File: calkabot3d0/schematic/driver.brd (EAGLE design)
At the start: 60.9 x 42.9 mm, 56 parts

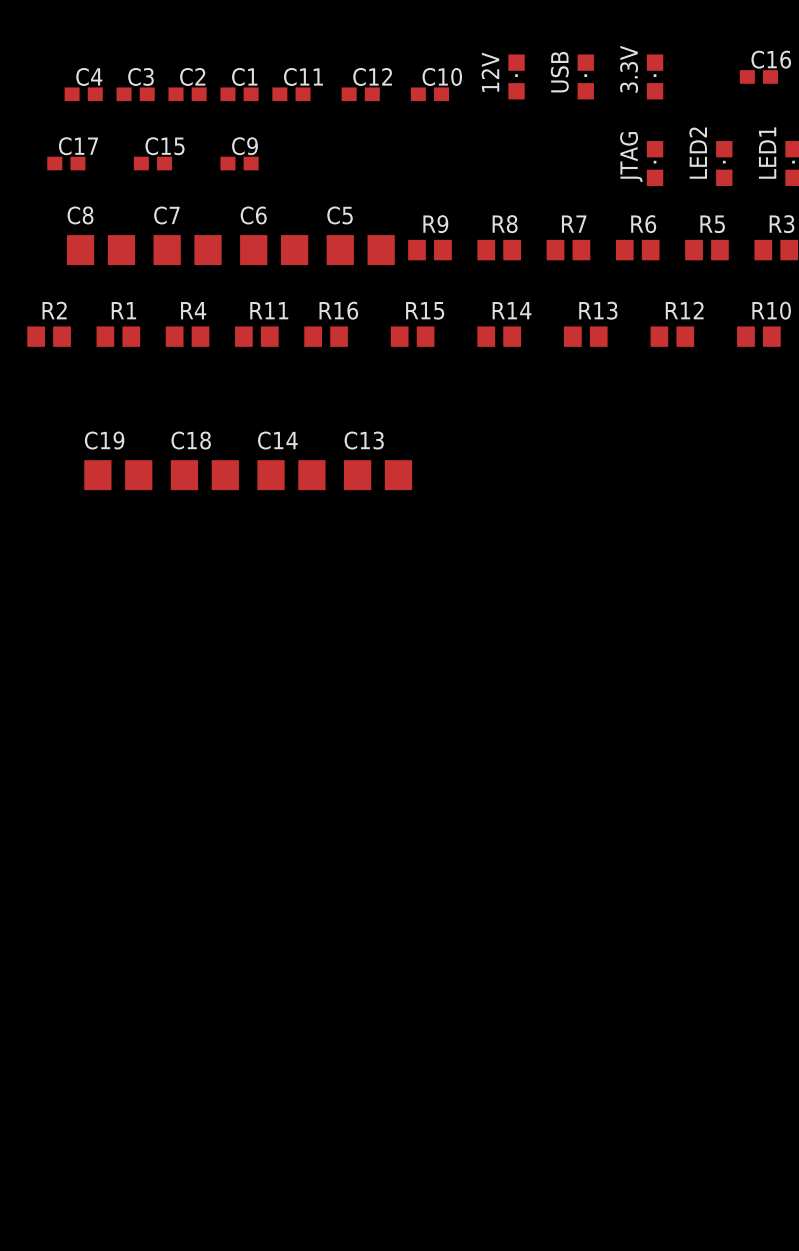
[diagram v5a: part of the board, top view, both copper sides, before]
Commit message: added battery voltage checker and led
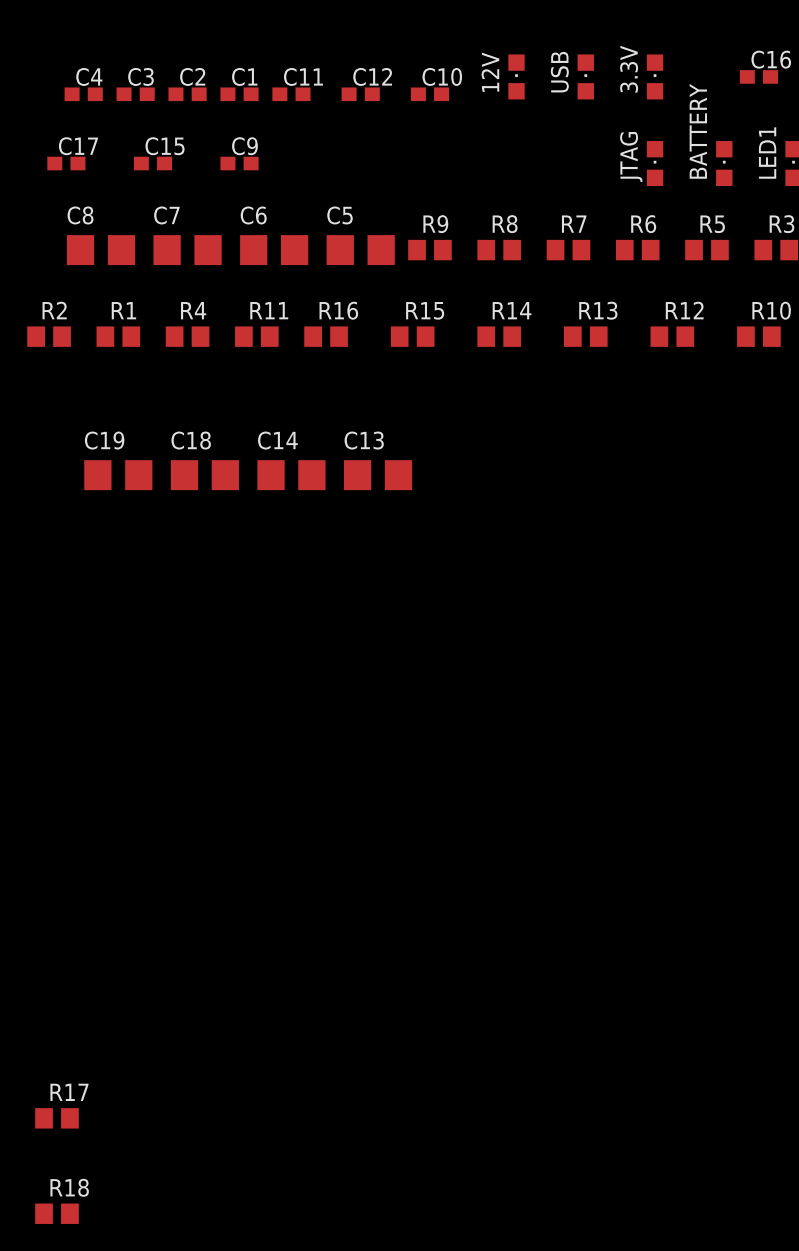
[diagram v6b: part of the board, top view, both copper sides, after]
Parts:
- added R17: 10k, rcl:R0805
- added R18: 30k, rcl:R0805
- renumbered LED2 to BATTERY
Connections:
- removed net S5: STM32.13
- new net BAT: R17.1, R18.2, STM32.13
- net GND: now also R18.1
- net STAB: now also R17.2
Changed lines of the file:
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@@
 <attribute name="VALUE" x="-11.43" y="64.77" size="1.27" layer="27" rot="R90"/>
 </element>
-<element name="LED2" library="led" library_urn="urn:adsk.eagle:library:259" package="CHIPLED_0805" package3d_urn="urn:adsk.eagle:package:15821/2" override_package3d_urn="urn:adsk.eagle:package:17628446/2" override_package_urn="urn:adsk.eagle:footprint:15685/1" value="" x="-19.05" y="66.04" smashed="yes">
+<element name="BATTERY" library="led" library_urn="urn:adsk.eagle:library:259" package="CHIPLED_0805" package3d_urn="urn:adsk.eagle:package:15821/2" override_package3d_urn="urn:adsk.eagle:package:17628446/2" override_package_urn="urn:adsk.eagle:footprint:15685/1" value="" x="-19.05" y="66.04" smashed="yes">
 <attribute name="NAME" x="-20.32" y="64.77" size="1.27" layer="25" rot="R90"/>
 <attribute name="POPULARITY" value="52" x="0" y="0" size="1.778" layer="27" display="off"/>
@@
 <attribute name="SPICEPREFIX" value="D" x="0" y="0" size="1.778" layer="27" display="off"/>
 <attribute name="VALUE" x="-26.67" y="71.12" size="1.27" layer="27" rot="R90"/>
+</element>
+<element name="R17" library="rcl" library_urn="urn:adsk.eagle:library:334" package="R0805" package3d_urn="urn:adsk.eagle:package:23553/2" value="10k" x="-68" y="-4" smashed="yes">
+<attribute name="NAME" x="-68.635" y="-2.73" size="1.27" layer="25"/>
+<attribute name="POPULARITY" value="86" x="-68" y="-4" size="1.778" layer="27" display="off"/>
+<attribute name="SPICEPREFIX" value="R" x="-68" y="-4" size="1.778" layer="27" display="off"/>
+<attribute name="VALUE" x="-68.635" y="-6.54" size="1.27" layer="27"/>
+</element>
+<element name="R18" library="rcl" library_urn="urn:adsk.eagle:library:334" package="R0805" package3d_urn="urn:adsk.eagle:package:23553/2" value="30k" x="-68" y="-11" smashed="yes">
+<attribute name="NAME" x="-68.635" y="-9.73" size="1.27" layer="25"/>
+<attribute name="POPULARITY" value="86" x="-68" y="-11" size="1.778" layer="27" display="off"/>
+<attribute name="SPICEPREFIX" value="R" x="-68" y="-11" size="1.778" layer="27" display="off"/>
+<attribute name="VALUE" x="-68.635" y="-13.54" size="1.27" layer="27"/>
 </element>
 </elements>
@@
 <contactref element="J2" pad="-"/>
 <contactref element="LED1" pad="C"/>
-<contactref element="LED2" pad="C"/>
+<contactref element="BATTERY" pad="C"/>
 <contactref element="JTAG" pad="C"/>
 <contactref element="USB" pad="C"/>
@@
 <wire x1="49.9826" y1="21.0174" x2="53" y2="18" width="1" layer="16"/>
 <wire x1="53" y1="18" x2="57" y2="18" width="1" layer="16"/>
+<contactref element="R18" pad="1"/>
 <wire x1="55.6166" y1="32.4485" x2="47.26" y2="35.29" width="0" layer="19" extent="1-1"/>
 <wire x1="30.48" y1="39.37" x2="47.26" y2="35.29" width="0" layer="19" extent="1-1"/>
@@
 <wire x1="-49.3" y1="43.18" x2="-55.65" y2="43.18" width="0" layer="19" extent="1-1"/>
 <wire x1="-42.95" y1="43.18" x2="-49.3" y2="43.18" width="0" layer="19" extent="1-1"/>
+<wire x1="-68.95" y1="-11" x2="-62" y2="43.18" width="0" layer="19" extent="1-1"/>
 </signal>
 <signal name="N$1">
@@
 <wire x1="57.51" y1="11.94" x2="58.94" y2="11.94" width="1" layer="16"/>
 <wire x1="58.94" y1="11.94" x2="59.424" y2="12.424" width="1" layer="16"/>
-<wire x1="-45.95" y1="43.18" x2="32.02" y2="35.29" width="0" layer="19" extent="1-1"/>
-<wire x1="-58.65" y1="43.18" x2="-45.95" y2="43.18" width="0" layer="19" extent="1-1"/>
+<contactref element="R17" pad="2"/>
+<wire x1="-58.65" y1="43.18" x2="-67.05" y2="-4" width="0" layer="19" extent="1-1"/>
 <wire x1="-57.47" y1="53.34" x2="-58.65" y2="43.18" width="0" layer="19" extent="1-1"/>
+<wire x1="-45.95" y1="43.18" x2="-58.65" y2="43.18" width="0" layer="19" extent="1-1"/>
+<wire x1="32.02" y1="35.29" x2="-45.95" y2="43.18" width="0" layer="19" extent="1-1"/>
 </signal>
 <signal name="LED1">
@@
 <contactref element="STM32" pad="14"/>
 </signal>
-<signal name="S5">
+<signal name="BAT">
 <contactref element="STM32" pad="13"/>
+<contactref element="R17" pad="1"/>
+<contactref element="R18" pad="2"/>
+<wire x1="-68.95" y1="-4" x2="-67.05" y2="-11" width="0" layer="19" extent="1-1"/>
+<wire x1="2.493478125" y1="50.767434375" x2="-68.95" y2="-4" width="0" layer="19" extent="1-16"/>
 </signal>
 <signal name="SWDA">
@@
 </signal>
 <signal name="N$8">
-<contactref element="LED2" pad="A"/>
+<contactref element="BATTERY" pad="A"/>
 <contactref element="R13" pad="1"/>
 <wire x1="-30.16" y1="53.34" x2="-19.05" y2="64.99" width="0" layer="19" extent="1-1"/>

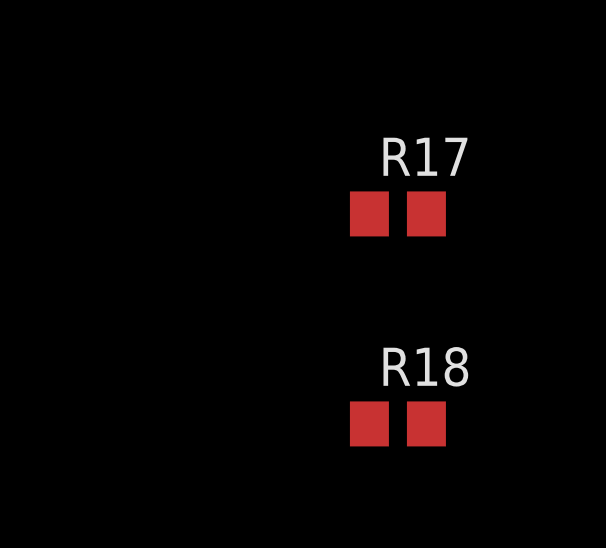
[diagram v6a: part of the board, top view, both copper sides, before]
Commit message: added switch to disconnect voltage from sensors
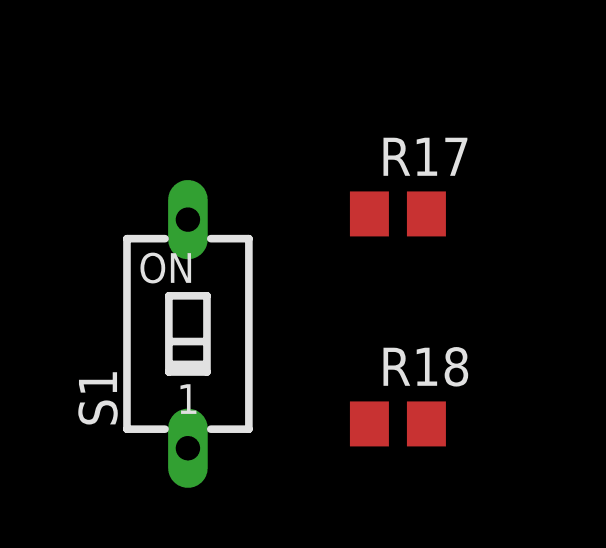
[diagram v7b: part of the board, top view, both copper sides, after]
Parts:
- added S1: (no value), switch-dil:SD4-01
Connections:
- new net VCC_S: I2C.4, S1.1
- net VCC: now also S1.2; no longer I2C.4
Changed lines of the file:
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@@
 <attribute name="VALUE" x="-68.635" y="-13.54" size="1.27" layer="27"/>
+</element>
+<element name="S1" library="switch-dil" library_urn="urn:adsk.eagle:library:375" package="SD4-01" package3d_urn="urn:adsk.eagle:package:27236/1" value="" x="-75" y="-8" smashed="yes">
+<attribute name="MF" value="" x="-75" y="-8" size="1.778" layer="27" display="off"/>
+<attribute name="MPN" value="" x="-75" y="-8" size="1.778" layer="27" display="off"/>
+<attribute name="NAME" x="-77.3622" y="-11.1242" size="1.27" layer="25" ratio="10" rot="R90"/>
+<attribute name="OC_FARNELL" value="unknown" x="-75" y="-8" size="1.778" layer="27" display="off"/>
+<attribute name="OC_NEWARK" value="unknown" x="-75" y="-8" size="1.778" layer="27" display="off"/>
+<attribute name="VALUE" x="-71.3678" y="-11.1496" size="1.27" layer="27" ratio="10" rot="R90"/>
 </element>
 </elements>
@@
 <contactref element="LM1" pad="4"/>
 <contactref element="C19" pad="+"/>
-<contactref element="I2C" pad="4"/>
 <contactref element="R16" pad="2"/>
 <contactref element="R15" pad="2"/>
 <wire x1="57.51" y1="14.24" x2="51.71" y2="14.24" width="1" layer="16"/>
+<contactref element="S1" pad="2"/>
 <wire x1="39.64" y1="22.59" x2="44.72" y2="35.29" width="0" layer="19" extent="1-1"/>
 <wire x1="51.71" y1="14.24" x2="39.64" y2="22.59" width="0" layer="19" extent="16-16"/>
-<wire x1="27.94" y1="39.37" x2="44.72" y2="35.29" width="0" layer="19" extent="1-1"/>
-<wire x1="-40.96" y1="53.34" x2="27.94" y2="39.37" width="0" layer="19" extent="1-1"/>
+<wire x1="-40.96" y1="53.34" x2="39.64" y2="22.59" width="0" layer="19" extent="1-1"/>
 <wire x1="-47.31" y1="53.34" x2="-40.96" y2="53.34" width="0" layer="19" extent="1-1"/>
 <wire x1="-65" y1="43.18" x2="-47.31" y2="53.34" width="0" layer="19" extent="1-1"/>
+<wire x1="-75" y1="-4.19" x2="-65" y2="43.18" width="0" layer="19" extent="1-1"/>
 </signal>
 <signal name="N$42">
@@
 <wire x1="-36.51" y1="59.69" x2="-29.21" y2="71.34" width="0" layer="19" extent="1-1"/>
 </signal>
+<signal name="VCC_S">
+<contactref element="S1" pad="1"/>
+<contactref element="I2C" pad="4"/>
+<wire x1="27.94" y1="39.37" x2="-75" y2="-11.81" width="0" layer="19" extent="1-1"/>
+</signal>
 </signals>

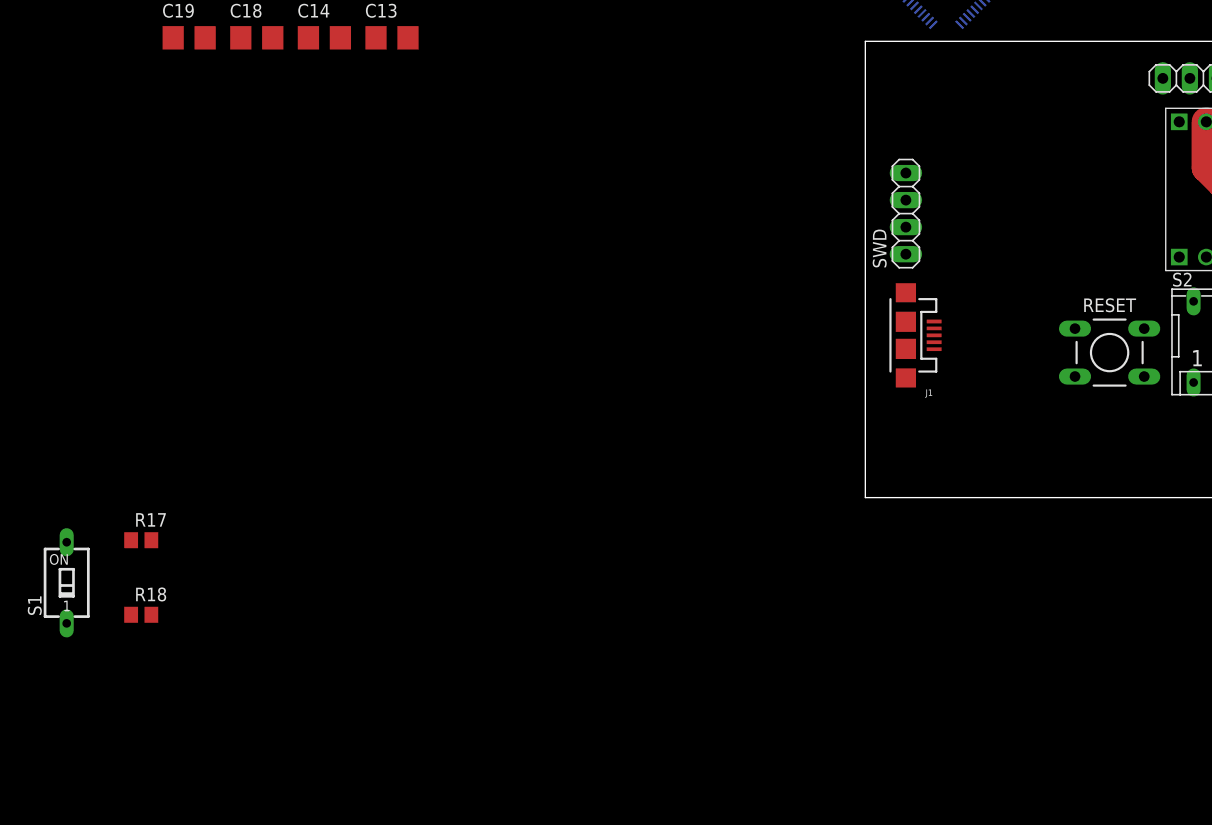
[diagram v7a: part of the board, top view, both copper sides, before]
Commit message: comments on schematic, added led for I2C supply
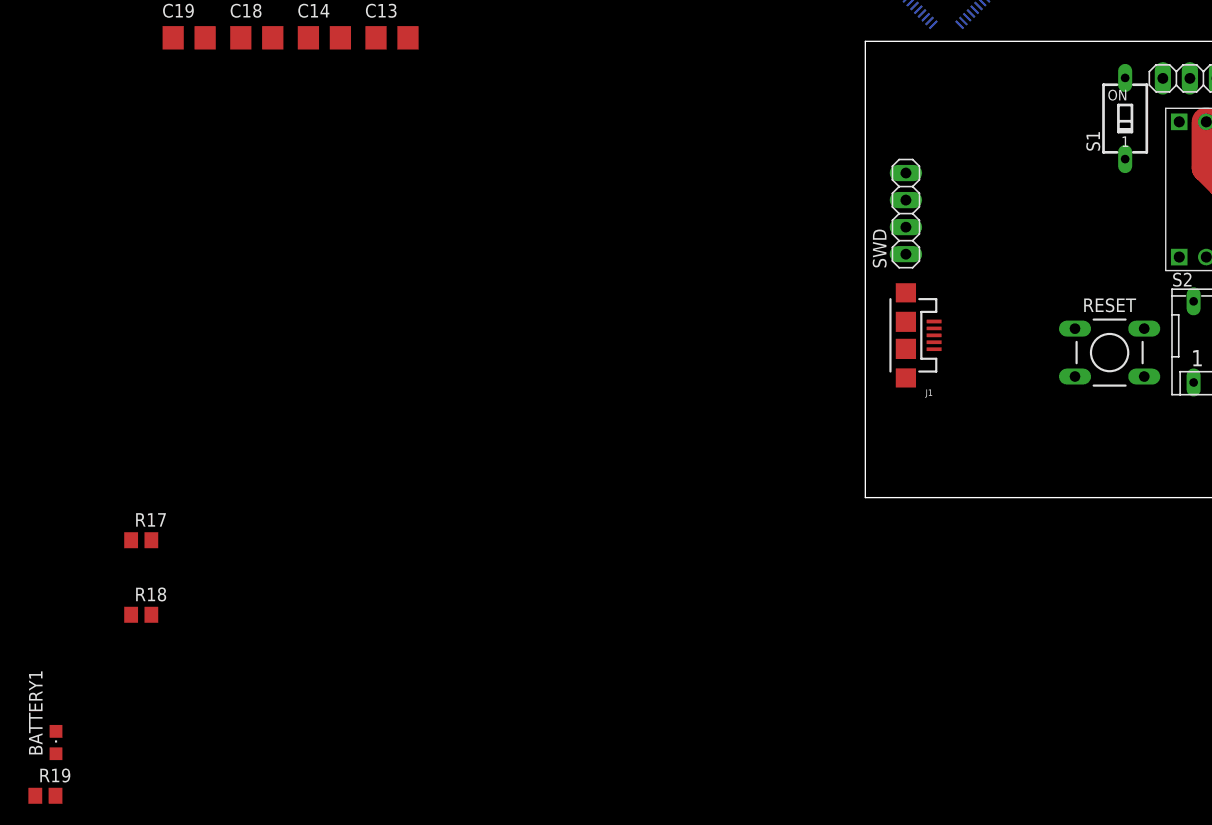
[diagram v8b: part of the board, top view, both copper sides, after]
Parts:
- added BATTERY1: (no value), led:CHIPLED_0805
- added R19: 65, rcl:R0805
- moved S1 108.5 mm to (24.4, 35.6)
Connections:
- new net N$9: BATTERY1.A, R19.1
- net GND: now also BATTERY1.C
- net VCC_S: now also R19.2
